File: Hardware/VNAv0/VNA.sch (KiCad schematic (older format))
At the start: 28 parts, among them J1 USB_B_Micro, J2 USB_A, J3 Conn_ARM_SWD, J4 SMA, J5 SMA, J6 UART, U1 TPD2S017, U2 TPD2S017

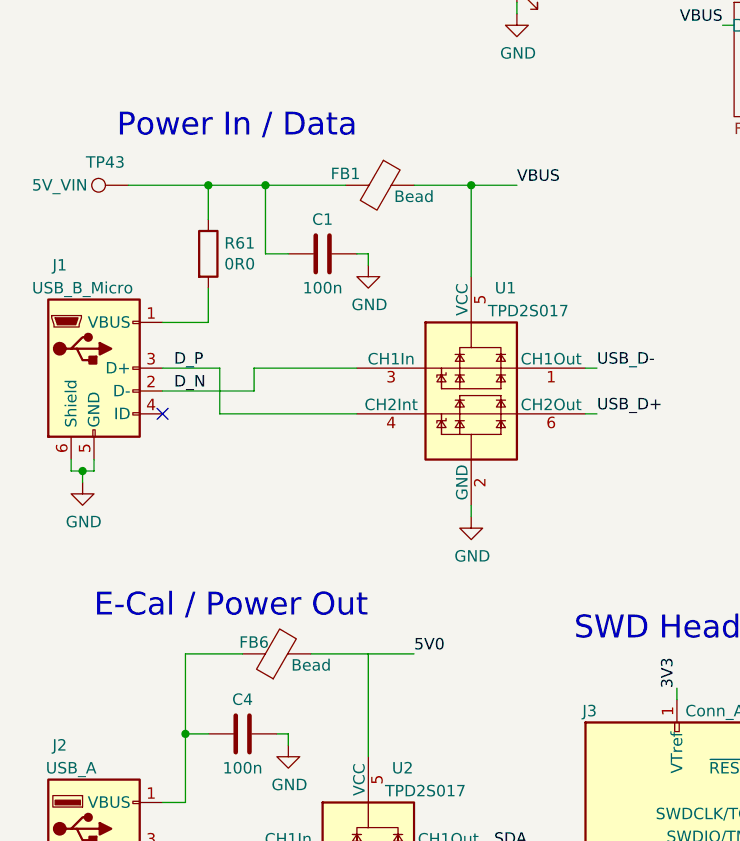
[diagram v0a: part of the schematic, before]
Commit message: tx chain now works, however output power too low
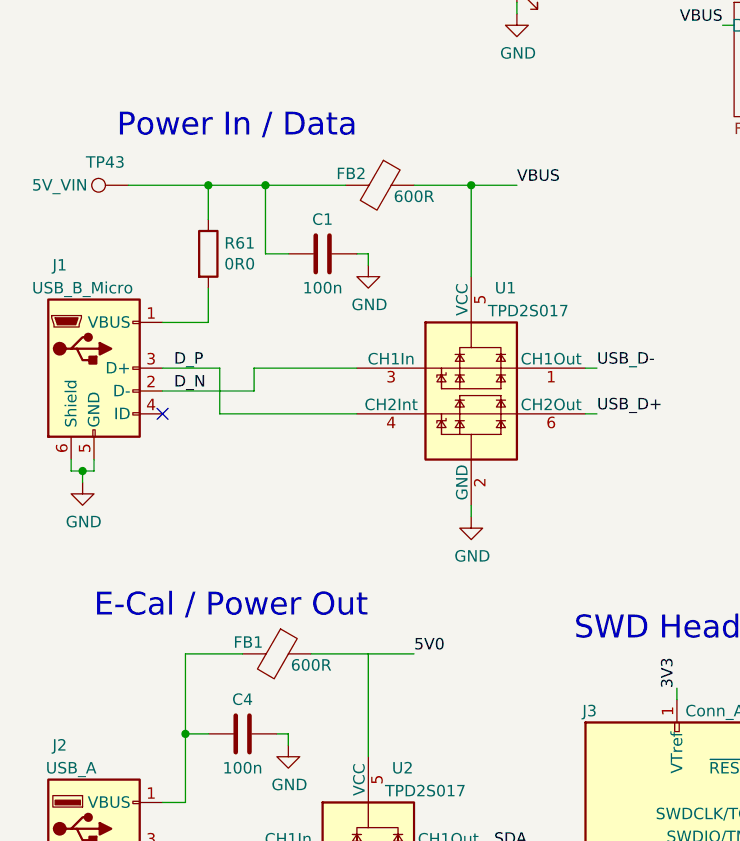
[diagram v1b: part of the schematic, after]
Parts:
- removed FB6: Bead, VNA_Footprints:BEADC1608X95N, symbol VNA_Symbols:Ferrite_Bead_PWR
- added FB2: 600R, symbol VNA_Symbols:Ferrite_Bead_PWR
- FB1: value Bead -> 600R; footprint VNA_Footprints:BEADC1608X95N -> (none)
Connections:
- net 5V0: now also FB1.1
- net VBUS: now also FB2.1; no longer FB1.1
- net at C1.1, R61.1, TP43.1: now also FB2.2; no longer FB1.2
- net at C4.1, J2.1 (VBUS): now also FB1.2
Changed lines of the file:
@@
 Text Label 5250 4300 2    50   ~ 0
 AD8302_VPHASE
-$Comp
-L VNA_Symbols:Ferrite_Bead_PWR FB1
-U 1 1 5CC56F48
-P 2100 3900
-F 0 "FB1" V 2050 3750 50  0000 C CNN
-F 1 "Bead" V 2150 4050 50  0000 C CNN
-F 2 "VNA_Footprints:BEADC1608X95N" V 2030 3900 50  0001 C CNN
-F 3 "~" H 2100 3900 50  0001 C CNN
-	1    2100 3900
-	0    1    1    0
-$EndComp
 Wire Wire Line
 	2500 3900 2700 3900
@@
 Text Notes 5500 6650 0    100  ~ 0
 Mounting Holes
-$Comp
-L VNA_Symbols:Ferrite_Bead_PWR FB6
-U 1 1 5CB8C1DA
-P 1650 5950
-F 0 "FB6" V 1700 6050 50  0000 C CNN
-F 1 "Bead" V 1600 5800 50  0000 C CNN
-F 2 "VNA_Footprints:BEADC1608X95N" V 1580 5950 50  0001 C CNN
-F 3 "~" H 1650 5950 50  0001 C CNN
-	1    1650 5950
-	0    -1   -1   0
-$EndComp
 Wire Wire Line
 	1800 5950 2050 5950
@@
 Text Notes 4450 3850 0    50   ~ 0
 NOTE: TX/\nRX swapped
+$Comp
+L VNA_Symbols:Ferrite_Bead_PWR FB2
+U 1 1 5D192DD5
+P 2100 3900
+F 0 "FB2" V 2050 3775 50  0000 C CNN
+F 1 "600R" V 2150 4050 50  0000 C CNN
+F 2 "" V 2030 3900 50  0001 C CNN
+F 3 "~" H 2100 3900 50  0001 C CNN
+	1    2100 3900
+	0    1    1    0
+$EndComp
+$Comp
+L VNA_Symbols:Ferrite_Bead_PWR FB1
+U 1 1 5D19418B
+P 1650 5950
+F 0 "FB1" V 1600 5825 50  0000 C CNN
+F 1 "600R" V 1700 6100 50  0000 C CNN
+F 2 "" V 1580 5950 50  0001 C CNN
+F 3 "~" H 1650 5950 50  0001 C CNN
+	1    1650 5950
+	0    1    1    0
+$EndComp
 $EndSCHEMATC
